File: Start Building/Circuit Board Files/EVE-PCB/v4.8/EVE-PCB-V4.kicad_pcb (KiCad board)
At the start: 4 copper layers, 103.5 x 90.6 mm, 102 parts, among them J1 PJ-102AH, J2 2x20 Male Header, J3 1725669, Q1 UA7805CKCT, Q10 DMN6140LQ-7, Q11 DMN6140LQ-7, Q12 DMN6140LQ-7, Q2 ULN2803ADWR, Q3 ULN2803ADWR, Q4 ULN2803ADWR, Q5 ULN2803ADWR, Q6 DMN6140LQ-7, Q7 DMN6140LQ-7, Q8 DMN6140LQ-7, Q9 DMN6140LQ-7, U1 PCA9685PW, U2 ADS1115IDGSR, U3 TLV4314IPWR, U4 TLV4314IPWR, U5 MCP1501-40E_SN, U7 MCP23017-E/SO, U8 MCP23017-E/SO

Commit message: Bump PCB version to 4.81
- Fixed voltages for fan and LED
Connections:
- L1 pad 10: +5V -> +12V
- L1 pad 11: +12V -> +5V
- L2 pad 10: +5V -> +12V
- L2 pad 11: +12V -> +5V
- L3 pad 10: +5V -> +12V
- L3 pad 11: +12V -> +5V
- L4 pad 10: +5V -> +12V
- L4 pad 11: +12V -> +5V
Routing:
- net +5V: track 74.5 -> 73.8 mm
- net +12V: track 62.0 -> 62.6 mm

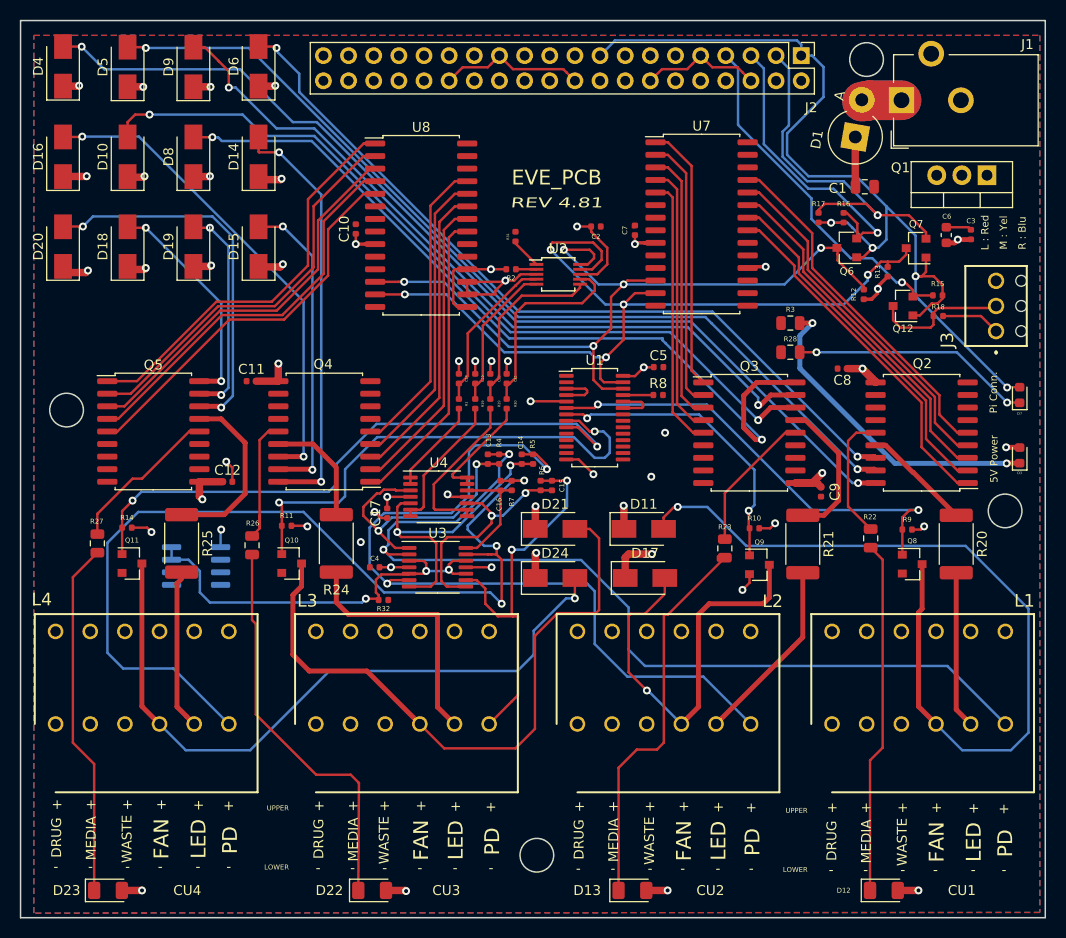
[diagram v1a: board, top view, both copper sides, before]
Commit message: Bump PCB to version 4.82
- Update schematic to use V_ref as PD positive terminal.
- Update PCB to allow for this change.
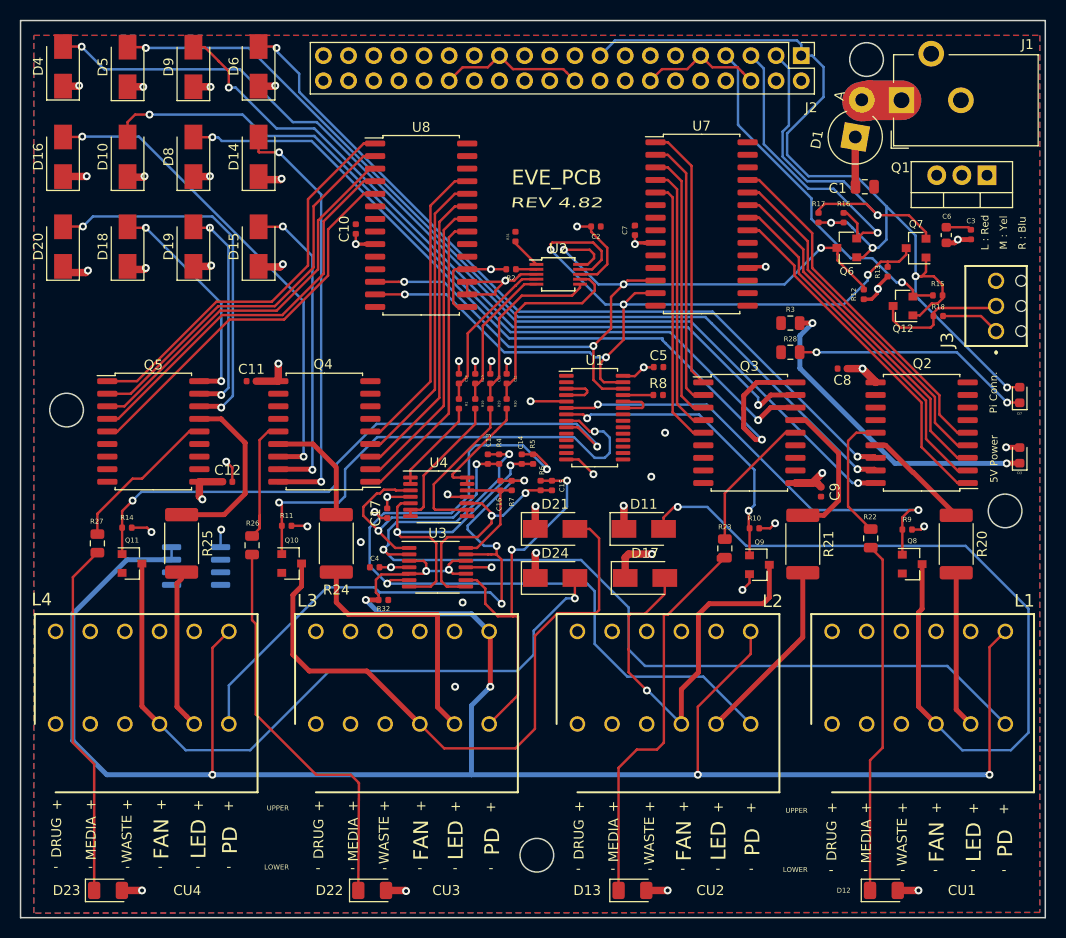
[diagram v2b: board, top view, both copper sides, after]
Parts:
- U5: value MCP1501-40E_SN -> MCP1501-10E/SN
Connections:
- L1 pad 12: GND -> /V_REF
- L2 pad 12: GND -> /V_REF
- L3 pad 12: GND -> /V_REF
- L4 pad 12: GND -> /V_REF
- R32 pad 2: /VREF -> /V_REF
- U3 pad 10: /VREF -> /V_REF
- U3 pad 12: /VREF -> /V_REF
- U3 pad 3: /VREF -> /V_REF
- U3 pad 5: /VREF -> /V_REF
- U5 pad 7: /VREF -> /V_REF
- U5 pad 8: /VREF -> /V_REF
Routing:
- net /V_REF: track 0.00 -> 214.7 mm, vias 0 -> 7
- net /VREF: track 42.2 -> 0.00 mm, vias 3 -> 0
- net /PD4_NEG: track 94.5 -> 59.4 mm
- net GND: track 79.2 -> 76.3 mm, vias 13 -> 15
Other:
- board text added: "REV 4.82"
- board text removed: "REV 4.81"
